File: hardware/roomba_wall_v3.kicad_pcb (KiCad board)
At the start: 2 copper layers, 31 x 30.5 mm, 17 parts, among them CON1 AVR-ISP-6, IC1 MIC5225-3.3, J1 USB_OTG, J2 JSTPH, J3 JSTPH, Q1 Q_NPN_BEC, U1 ATTINY45-20SU, Y1 8Mhz

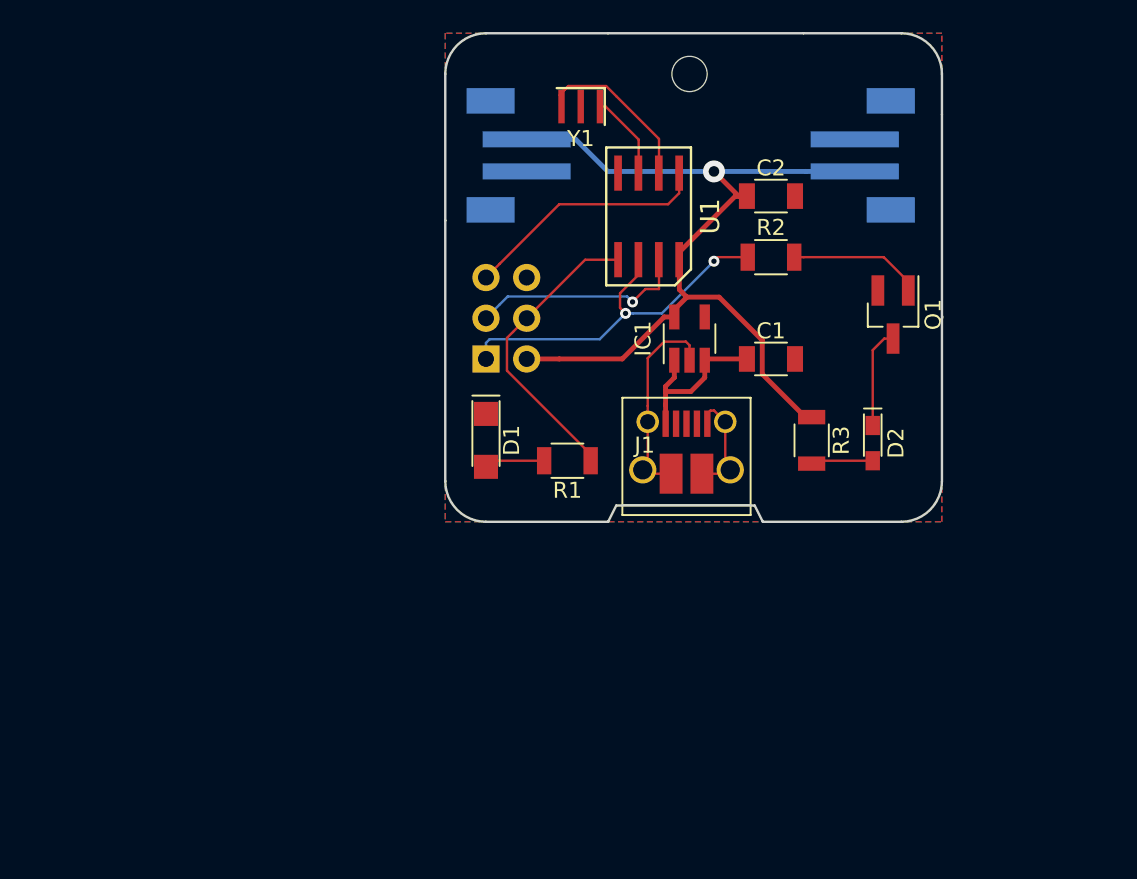
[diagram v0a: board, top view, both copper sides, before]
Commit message: Updated footprint associations, etc for v3
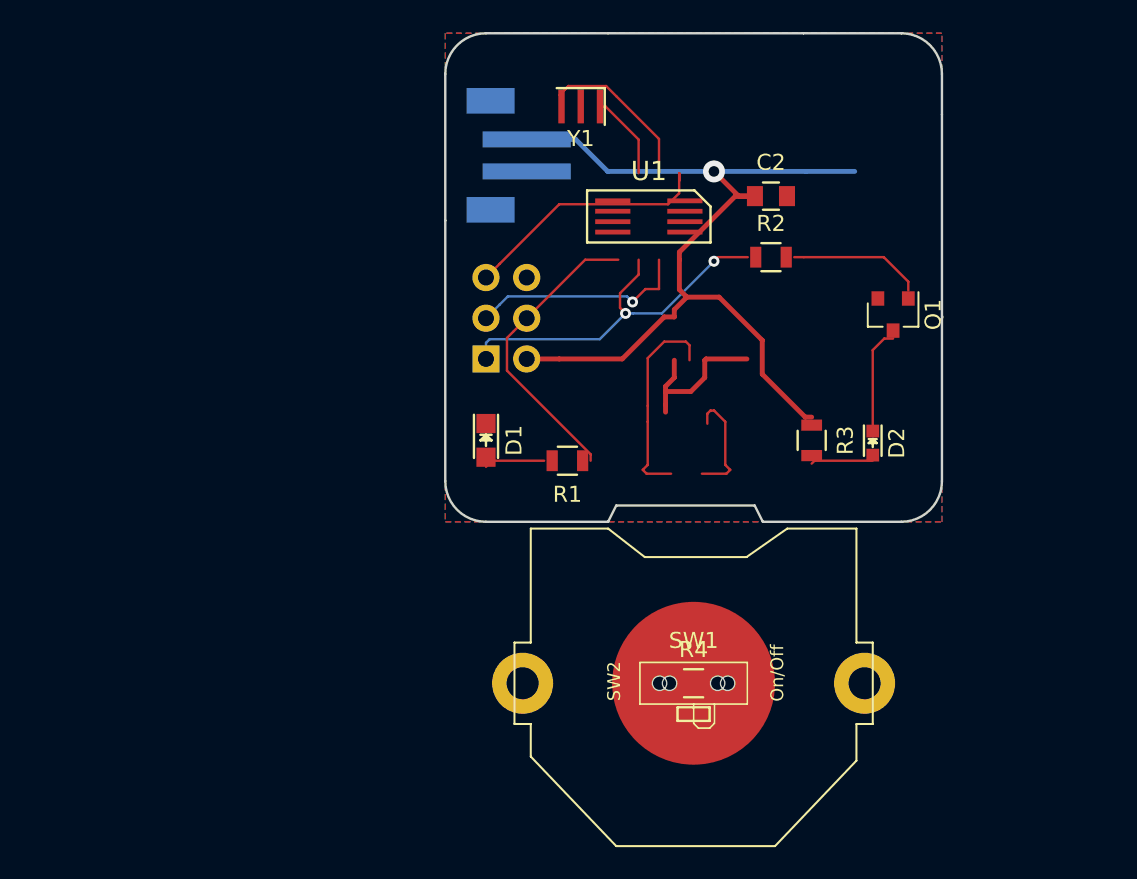
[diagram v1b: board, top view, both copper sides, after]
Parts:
- removed C1: 10uF, lib_fp:C_1206
- removed G***: LOGO, kicad-libs:petezah-logo-tiny
- removed IC1: MIC5225-3.3, lib_fp:SOT-23-5_HandSoldering
- removed J1: USB_OTG, lib_fp:USB_Micro-B_10103594-0001LF
- removed J3: JSTPH, lib_fp:JST_PH_B2B-PH-SM4-TB_02x2.00mm_Straight
- removed REF**: MountingHole_2.2mm_M2, Mounting_Holes:MountingHole_2.2mm_M2
- added BT1: Battery_Cell, kicad-libs:CR2032-THRU, F.Cu at (160.3, 144.7)
- added R4: 10k, Resistors_SMD:R_0805, F.Cu at (160.3, 144.7)
- added SW1: Button, kicad-libs:e-switch-TL-3340-AF160QG, F.Cu at (160.3, 144.7)
- added SW2: On/Off, kicad-libs:SSSS810701, F.Cu at (160.3, 144.7)
- C2: footprint lib_fp:C_1206 -> Capacitors_SMD:C_0805
- D1: footprint lib_fp:LED_1206 -> LEDs:LED_0805
- D2: footprint lib_fp:LED_0603_HandSoldering -> LEDs:LED_0603
- Q1: footprint lib_fp:SOT-23_Handsoldering -> TO_SOT_Packages_SMD:SOT-23
- R1, R2, R3: footprint lib_fp:R_1206 -> Resistors_SMD:R_0805
- U1: footprint lib_fp:SOIC-8_5.35x5.40mm_Pitch1.27mm -> kicad-libs:ATtiny45V-10XU-TSSOP-8
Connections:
- net /SCK renamed /SCK/BUTTON
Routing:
- net (no net): track 0.00 -> 38.5 mm
- net GND: track 20.1 -> 0.00 mm
- net VBUS: track 10.0 -> 0.00 mm
- net Net-(Q1-Pad1): track 8.30 -> 0.00 mm

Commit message: Fix fp archive pointers
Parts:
- BT1: footprint kicad-libs:CR2032-THRU -> lib_fp:CR2032-THRU
- C2: footprint Capacitors_SMD:C_0805 -> lib_fp:C_0805
- D1: footprint LEDs:LED_0805 -> lib_fp:LED_0805
- D2: footprint LEDs:LED_0603 -> lib_fp:LED_0603
- Q1: footprint TO_SOT_Packages_SMD:SOT-23 -> lib_fp:SOT-23
- R1, R2, R3, R4: footprint Resistors_SMD:R_0805 -> lib_fp:R_0805
- SW1: footprint kicad-libs:e-switch-TL-3340-AF160QG -> lib_fp:e-switch-TL-3340-AF160QG
- SW2: footprint kicad-libs:SSSS810701 -> lib_fp:SSSS810701
- U1: footprint kicad-libs:ATtiny45V-10XU-TSSOP-8 -> lib_fp:ATtiny45V-10XU-TSSOP-8
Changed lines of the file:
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@@
-(kicad_pcb (version 4) (host pcbnew 4.0.6)
+(kicad_pcb (version 4) (host pcbnew 4.0.7)
   (general
     (links 31)
@@
   (page A4)
   (title_block
-    (title "Roomba Christmas Tree Barrier")
-    (date 2018-01-03)
-    (rev B)
+    (title "Roomba Wall V3")
+    (date 2018-03-03)
+    (rev A)
     (company Petezah)
-    (comment 1 "(C) 2017 Peter Dunshee")
+    (comment 1 "(C) 2018 Peter Dunshee")
   )
   (layers
@@
       (net 10 "Net-(U1-Pad3)"))
   )
-  (module kicad-libs:CR2032-THRU (layer F.Cu)
+  (module lib_fp:CR2032-THRU (layer F.Cu)
     (at 160.274 144.695001)
     (tags "cr2032 battery th")
@@
       (net 1 GND))
   )
-  (module Capacitors_SMD:C_0805 (layer F.Cu)
+  (module lib_fp:C_0805 (layer F.Cu)
     (at 165.1 114.3)
     (descr "Capacitor SMD 0805, reflow soldering, AVX (see smccp.pdf)")
@@
     )
   )
-  (module LEDs:LED_0805 (layer F.Cu)
+  (module lib_fp:LED_0805 (layer F.Cu)
     (at 147.32 129.54 270)
     (descr "LED 0805 smd package")
@@
     )
   )
-  (module LEDs:LED_0603 (layer F.Cu)
+  (module lib_fp:LED_0603 (layer F.Cu)
     (at 171.45 129.71 270)
     (descr "LED 0603 smd package")
@@
     )
   )
-  (module TO_SOT_Packages_SMD:SOT-23 (layer F.Cu)
+  (module lib_fp:SOT-23 (layer F.Cu)
     (at 172.72 121.69 270)
     (descr "SOT-23, Standard")
@@
     )
   )
-  (module Resistors_SMD:R_0805 (layer F.Cu)
+  (module lib_fp:R_0805 (layer F.Cu)
     (at 152.4 130.81 180)
     (descr "Resistor SMD 0805, reflow soldering, Vishay (see dcrcw.pdf)")
@@
     )
   )
-  (module Resistors_SMD:R_0805 (layer F.Cu)
+  (module lib_fp:R_0805 (layer F.Cu)
     (at 165.1 118.11)
     (descr "Resistor SMD 0805, reflow soldering, Vishay (see dcrcw.pdf)")
@@
     )
   )
-  (module Resistors_SMD:R_0805 (layer F.Cu)
+  (module lib_fp:R_0805 (layer F.Cu)
     (at 167.64 129.54 270)
     (descr "Resistor SMD 0805, reflow soldering, Vishay (see dcrcw.pdf)")
@@
     )
   )
-  (module Resistors_SMD:R_0805 (layer F.Cu)
+  (module lib_fp:R_0805 (layer F.Cu)
     (at 160.274 144.695001)
     (descr "Resistor SMD 0805, reflow soldering, Vishay (see dcrcw.pdf)")
@@
     )
   )
-  (module kicad-libs:e-switch-TL-3340-AF160QG (layer F.Cu)
+  (module lib_fp:e-switch-TL-3340-AF160QG (layer F.Cu)
     (at 160.274 144.695001)
     (descr https://www.mouser.com/ds/2/140/TL3340-346332.pdf)
@@
     (pad "" np_thru_hole circle (at -2.125 0) (size 0.9 0.9) (drill 0.9) (layers *.Cu *.Mask))
   )
-  (module kicad-libs:SSSS810701 (layer F.Cu)
+  (module lib_fp:SSSS810701 (layer F.Cu)
     (at 160.274 144.695001)
     (descr http://www.alps.com/prod/info/E/HTML/Switch/Slide/SSSS8/SSSS810701.html)
@@
     (pad "" smd rect (at 3.65 1.1) (size 1 0.8) (layers F.Cu F.Paste F.Mask))
   )
-  (module kicad-libs:ATtiny45V-10XU-TSSOP-8 (layer F.Cu)
+  (module lib_fp:ATtiny45V-10XU-TSSOP-8 (layer F.Cu)
     (at 157.48 115.57 270)
     (descr http://ww1.microchip.com/downloads/en/DeviceDoc/Atmel-2586-AVR-8-bit-Microcontroller-ATtiny25-ATtiny45-ATtiny85_Datasheet.pdf)

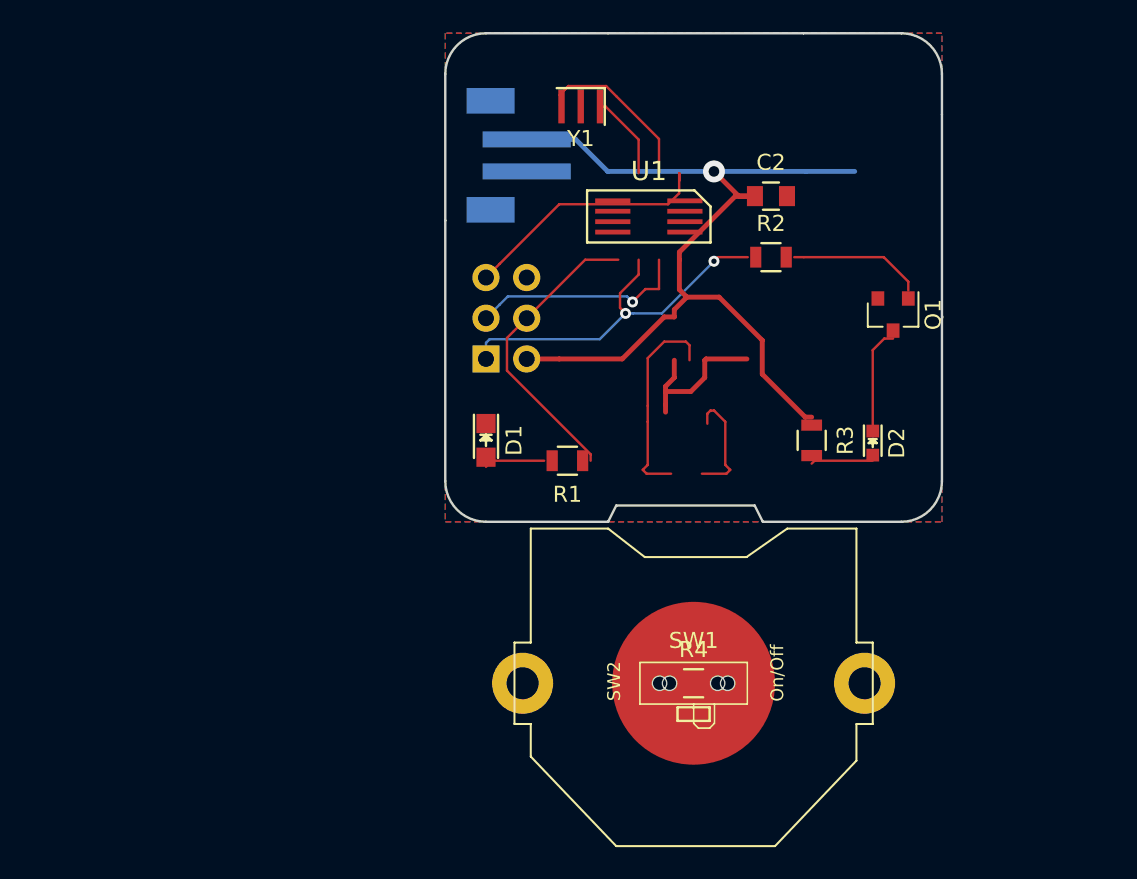
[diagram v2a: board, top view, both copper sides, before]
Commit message: Fix all ERC errors
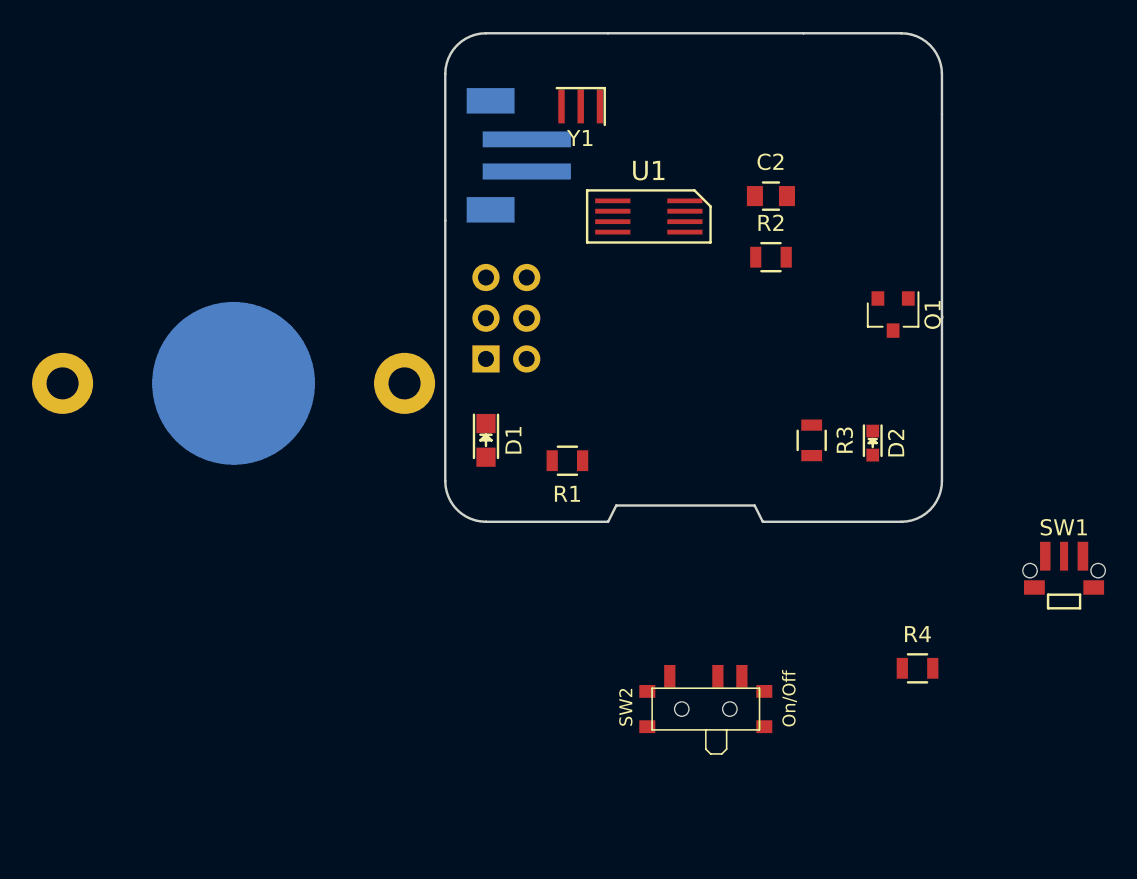
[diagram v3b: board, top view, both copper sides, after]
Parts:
- BT1: moved to B.Cu
- moved BT1 34.3 mm to (131.6, 126.0)
- moved SW1 24.2 mm to (183.4, 137.7)
- moved R4 14.0 mm to (174.2, 143.8)
- moved SW2 1.78 mm to (161.0, 146.3)
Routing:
- net +3V3: track 56.6 -> 0.00 mm, vias 1 -> 0
- net (no net): track 38.5 -> 0.00 mm
- net /MISO/IR: track 23.5 -> 0.00 mm, vias 2 -> 0
- net /MOSI/INDICATOR: track 18.8 -> 0.00 mm
- net /RST: track 16.0 -> 0.00 mm
- net /SCK/BUTTON: track 13.7 -> 0.00 mm, vias 1 -> 0
- net Net-(U1-Pad2): track 11.4 -> 0.00 mm
- net Net-(D2-Pad1): track 6.27 -> 0.00 mm
- net Net-(U1-Pad3): track 5.36 -> 0.00 mm
- net Net-(D2-Pad2): track 3.88 -> 0.00 mm
- net Net-(D1-Pad2): track 3.79 -> 0.00 mm
- removed copper zone on B.Cu, net GND
- removed copper zone on F.Cu, net GND

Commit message: Placed and routed new PCB layout
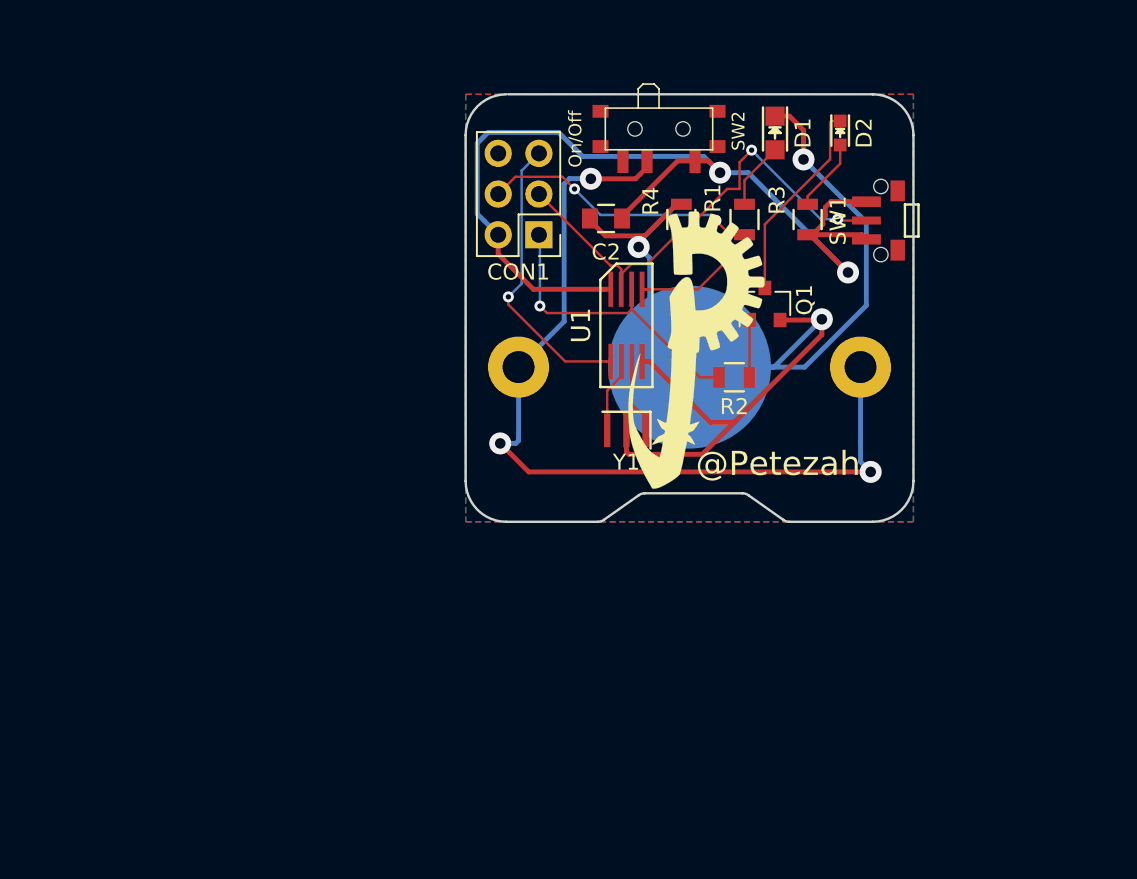
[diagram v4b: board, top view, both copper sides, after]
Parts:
- removed J2: JSTPH, lib_fp:JST_PH_B2B-PH-SM4-TB_02x2.00mm_Straight
- added G***: LOGO, lib_fp:petezah-logo-tiny, F.Cu at (160.5, 124.0)
- CON1: moved to F.Cu
- moved SW2 36.3 mm to (158.1, 110.1), turned to 180 degrees
- moved R4 31.6 mm to (159.5, 115.8), turned to 90 degrees
- moved BT1 28.5 mm to (160.0, 125.0)
- moved D1 26.3 mm to (165.4, 110.4)
- moved SW1 24.7 mm to (172.0, 115.8), turned to 90 degrees
- moved Y1 20.4 mm to (156.1, 128.9)
- moved D2 19.5 mm to (169.4, 110.4)
- moved R1 18.7 mm to (163.4, 115.8), turned to 90 degrees
- moved R3 13.8 mm to (167.4, 115.8), turned to 90 degrees
- moved C2 10.4 mm to (154.8, 115.7), turned to 180 degrees
- moved CON1 8.42 mm to (150.6, 116.7), turned to 180 degrees
- moved Q1 8.03 mm to (164.7, 121.0), turned to 90 degrees
- moved R2 7.83 mm to (162.8, 125.6)
- moved U1 6.94 mm to (156.1, 122.4), turned to 0 degrees
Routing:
- net GND: track 0.00 -> 83.9 mm, vias 0 -> 3
- net +3V3: track 0.00 -> 62.5 mm, vias 0 -> 2
- net VBAT: track 0.00 -> 55.1 mm, vias 0 -> 3
- net /SCK/BUTTON: track 0.00 -> 30.8 mm, vias 0 -> 2
- net /MOSI/INDICATOR: track 0.00 -> 26.0 mm, vias 0 -> 2
- net /MISO/IR: track 0.00 -> 18.9 mm, vias 0 -> 1
- net /RST: track 0.00 -> 18.1 mm, vias 0 -> 1
- net Net-(D2-Pad1): track 0.00 -> 12.7 mm
- net Net-(U1-Pad3): track 0.00 -> 4.72 mm
- net Net-(U1-Pad2): track 0.00 -> 4.65 mm
- net Net-(D2-Pad2): track 0.00 -> 4.54 mm
- net Net-(D1-Pad2): track 0.00 -> 4.19 mm
- net Net-(Q1-Pad1): track 0.00 -> 3.57 mm
- added copper zone on B.Cu, net GND
- added copper zone on F.Cu, net GND
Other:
- board size 31 x 30.5 mm -> 27.9 x 26.7 mm
- board text added: "Roomba Wall v3, Rev A (C) Copyright 2018 Peter Dunshee @Petezah"
- board text removed: "Roomba Christmas Tree Barrier (C) Copyright 2017 Peter Dunshee @Petezah"
